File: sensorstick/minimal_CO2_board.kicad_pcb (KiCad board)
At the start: 2 copper layers, 80 x 28 mm, 4 parts, among them J1 USB_A, U1 ESP32-C3_SUPERMINI

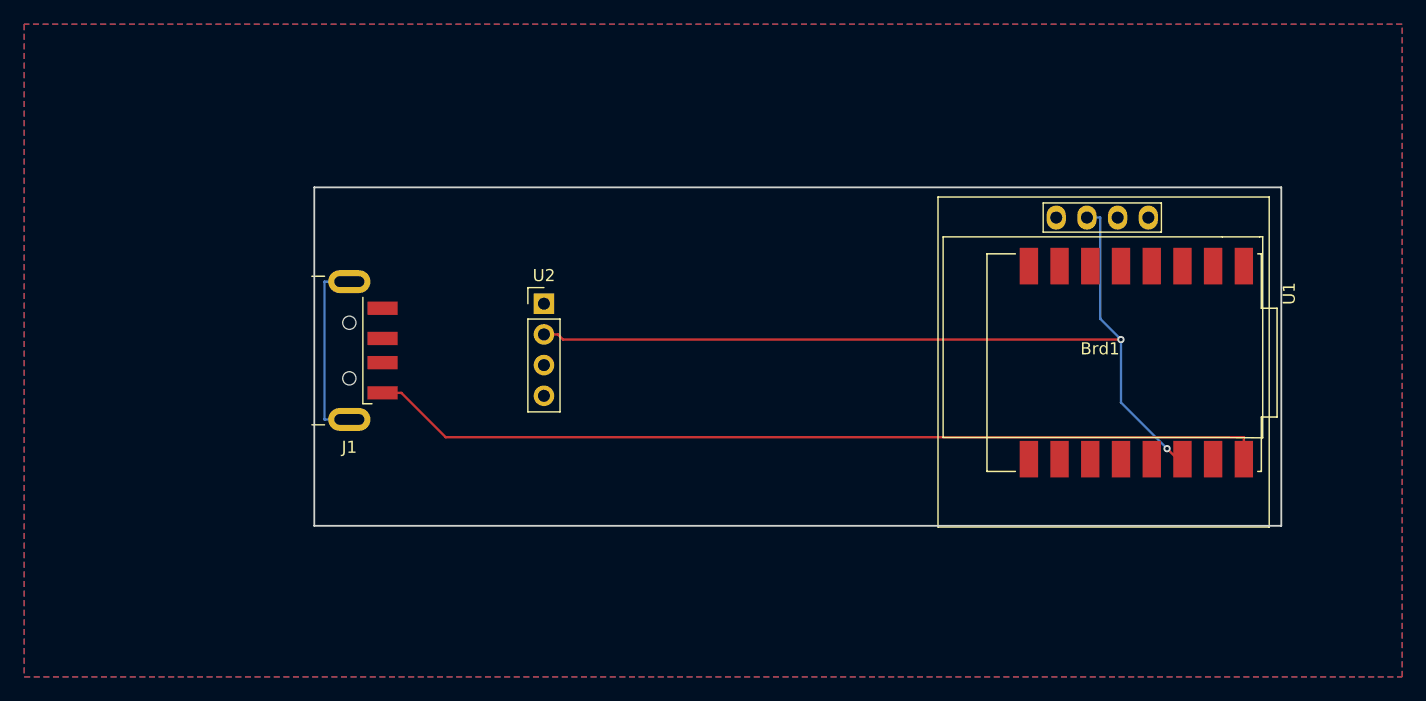
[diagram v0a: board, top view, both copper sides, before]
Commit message: add battery
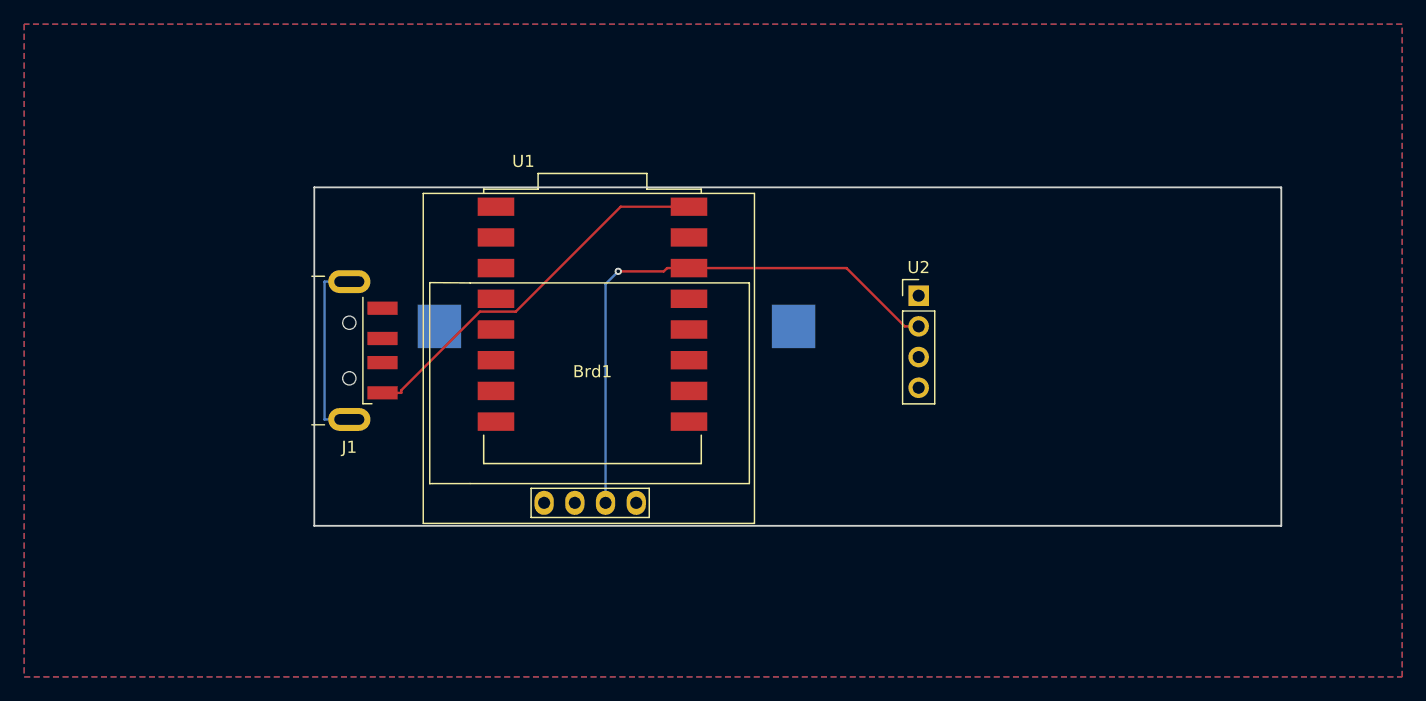
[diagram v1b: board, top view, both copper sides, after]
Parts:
- added BT1: Battery_Cell, CustomLibrary:BatteryHolder_Keystone_1060_1x2032, B.Cu at (85.0, 99.0)
- moved U1 44.1 mm to (83.0, 99.0), turned to 0 degrees
- moved Brd1 42.1 mm to (83.0, 103.0), turned to 180 degrees
- moved U2 31.0 mm to (110.0, 96.5)
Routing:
- net +5V: track 74.6 -> 31.9 mm
- net +3.3V: track 72.0 -> 46.5 mm, vias 2 -> 1

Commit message: add stuff
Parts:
- removed Brd1: SSD1306, CustomLibrary:128x64OLED
- removed J1: USB_A, Connector_USB:USB_A_CNCTech_1001-011-01101_Horizontal
- added OLED1: HS91L02W2C01, CustomLibrary:OLED-TH_L38.0-W12.0_HS91L02W2C01, F.Cu at (91.0, 98.5)
- added USB1: U217-04XN-XXR84, CustomLibrary:USB-A-SMD_U217-041N-4BV81, F.Cu at (64.3, 98.5)
- moved BT1 29.5 mm to (114.5, 99.0)
- moved U2 24.8 mm to (132.1, 107.8), turned to 90 degrees
- moved U1 5.52 mm to (77.5, 99.0)
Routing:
- net +3.3V: track 46.5 -> 85.7 mm, vias 1 -> 2
- net +5V: track 31.9 -> 14.8 mm, vias 0 -> 1
- net unconnected-(J1-Shield-Pad5): track 15.5 -> 0.00 mm
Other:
- board size 80 x 28 mm -> 85 x 23 mm
